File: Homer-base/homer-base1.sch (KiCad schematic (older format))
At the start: 13 parts, among them J1 J1 LEFT, J2 J2 DOWN, J3 J3 RIGHT

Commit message: Add level converter and other fix
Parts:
- removed P?: CONN_6, symbol CONN_6
- added P?: CONN_5, symbol CONN_5
- added U?: DCDC, symbol DCDC
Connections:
- net labels added: +3.6V
- wire segments 62 -> 81
- no-connect marks 0 -> 1
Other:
- moved on the sheet: C?, J?, JP?, U?

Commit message: New power supply subsystem
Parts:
- removed P?: CONN_5, symbol CONN_5
- added JP?: JUMPER, symbol JUMPER
- added P?: CONN_4, symbol CONN_4
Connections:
- net labels added: 3,3V
- net labels removed: +3,3V
- no-connect marks 1 -> 0
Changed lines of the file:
@@
 LIBS:valves
 LIBS:MyKicadLib
+LIBS:molex
 LIBS:homer-base1-cache
 EELAYER 27 0
@@
 Sheet 1 1
 Title ""
-Date "1 jan 2016"
+Date "12 feb 2017"
 Rev ""
 Comp ""
@@
 Connection ~ 6950 1450
 Wire Wire Line
-	3750 700  6650 700
-Wire Wire Line
 	6650 700  6650 950
 Wire Wire Line
@@
 Wire Wire Line
 	5200 5550 6600 5550
-Wire Wire Line
-	6300 5550 6300 5250
 Wire Wire Line
 	4900 2250 4650 2250
@@
 $EndComp
 $Comp
-L +3,3V #PWR?
-U 1 1 55470334
-P 6300 5250
-F 0 "#PWR?" H 6300 5210 30  0001 C CNN
-F 1 "+3,3V" H 6300 5360 30  0000 C CNN
-F 2 "" H 6300 5250 60  0001 C CNN
-F 3 "" H 6300 5250 60  0001 C CNN
-	1    6300 5250
-	1    0    0    -1
-$EndComp
-$Comp
 L GND #PWR?
 U 1 1 554702F9
@@
 $EndComp
 Wire Wire Line
-	1200 1100 1200 2950
+	1200 700  1200 2950
 $Comp
 L +3.3V #PWR?
@@
 $EndComp
 Wire Wire Line
-	1500 650  1500 3750
-Wire Wire Line
-	1500 700  1050 700
-Connection ~ 1500 700
+	1500 650  1500 3000
 Entry Wire Line
 	1500 3750 1600 3850
-Connection ~ 6300 5550
 Entry Wire Line
 	5100 5450 5200 5550
@@
 	3750 700  3750 2250
 Wire Wire Line
-	2450 2250 1500 2250
-Connection ~ 1500 2250
-Wire Wire Line
 	3450 2350 3750 2350
 Wire Wire Line
@@
 Wire Wire Line
 	3750 2750 1200 2750
-Connection ~ 1200 2750
 Wire Wire Line
 	2450 2350 2300 2350
@@
 	2300 2350 2300 2750
 Connection ~ 2300 2750
-$Comp
-L CONN_5 P?
-U 1 1 56866CB4
-P 650 900
-F 0 "P?" V 600 900 50  0000 C CNN
-F 1 "CONN_5" V 700 900 50  0000 C CNN
-F 2 "" H 650 900 60  0000 C CNN
-F 3 "" H 650 900 60  0000 C CNN
-	1    650  900
-	-1   0    0    -1
-$EndComp
-NoConn ~ 1050 1000
-Wire Wire Line
-	1200 1100 1050 1100
 $Comp
 L +3.6V #PWR?
@@
 $EndComp
 Wire Wire Line
-	1050 800  3750 800
-Connection ~ 3750 800
-Wire Wire Line
-	1650 800  1650 650
-Connection ~ 1650 800
+	1650 650  1650 1000
 $Comp
 L +3.6V #PWR?
@@
 	1    0    0    -1
 $EndComp
-Wire Wire Line
-	1050 900  1800 900
-Wire Wire Line
-	1800 900  1800 650
 Entry Wire Line
 	8300 1900 8400 2000
@@
 Wire Wire Line
 	10100 3000 10100 2950
+$Comp
+L JUMPER JP?
+U 1 1 58A04E2A
+P 1500 3300
+F 0 "JP?" H 1500 3450 60  0000 C CNN
+F 1 "JUMPER" H 1500 3220 40  0000 C CNN
+F 2 "" H 1500 3300 60  0001 C CNN
+F 3 "" H 1500 3300 60  0001 C CNN
+	1    1500 3300
+	0    1    1    0
+$EndComp
+Wire Wire Line
+	1500 3750 1500 3600
+Text Label 6350 5550 0    60   ~ 0
+3,3V
+Wire Wire Line
+	2450 2250 1500 2250
+Connection ~ 1500 2250
+$Comp
+L CONN_4 P?
+U 1 1 58A0935B
+P 650 850
+F 0 "P?" V 600 850 50  0000 C CNN
+F 1 "CONN_4" V 700 850 50  0000 C CNN
+F 2 "" H 650 850 60  0000 C CNN
+F 3 "" H 650 850 60  0000 C CNN
+	1    650  850
+	-1   0    0    -1
+$EndComp
+Connection ~ 3750 700
+Wire Wire Line
+	1800 650  1800 900
+Wire Wire Line
+	1650 700  6650 700
+Connection ~ 1200 2750
+Wire Wire Line
+	1200 700  1000 700
+Wire Wire Line
+	1650 1000 1000 1000
+Connection ~ 1650 700
+Wire Wire Line
+	1800 900  1000 900
+Wire Wire Line
+	1000 800  1500 800
+Connection ~ 1500 800
 $EndSCHEMATC

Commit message: Add current sensor, RTC battery, Power protection
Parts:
- added BT?: BATTERY, ~, symbol BATTERY
- added P?: BASE POWER, symbol CONN_8X2
- P?: value CONN_8X2 -> FRONT PANEL
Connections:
- net GND: now also BT?.2 (-)
- net PA30 TWD0: now also P?.2
- net PA31 TWCK0: now also P?.1
- net VBAT: now reaches J3.2 (P2)
- net VBAT: now also BT?.1 (+)
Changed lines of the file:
@@
 Sheet 1 1
 Title ""
-Date "12 feb 2017"
+Date "18 apr 2017"
 Rev ""
 Comp ""
@@
 	6900 2250 6500 2250
 Wire Wire Line
-	6950 1450 6950 1600
+	6950 850  6950 1600
 Connection ~ 6950 1450
 Wire Wire Line
@@
 	10800 3850 750  3850
 Wire Bus Line
-	10800 1850 10800 3850
+	10800 1850 10800 7000
 Wire Bus Line
 	8100 3950 8100 7000
@@
 	2400 5300 3000 5300
 Wire Bus Line
-	8300 1800 8300 3750
+	8300 700  8300 3750
 Entry Wire Line
 	3000 5400 3100 5500
@@
 P 9500 2350
 F 0 "P?" H 9500 2800 60  0000 C CNN
-F 1 "CONN_8X2" V 9500 2350 50  0000 C CNN
+F 1 "FRONT PANEL" V 9500 2350 50  0000 C CNN
 F 2 "" H 9500 2350 60  0001 C CNN
 F 3 "" H 9500 2350 60  0001 C CNN
@@
 	1000 800  1500 800
 Connection ~ 1500 800
+$Comp
+L CONN_8X2 P?
+U 1 1 58D59E38
+P 9550 5550
+F 0 "P?" H 9550 6000 60  0000 C CNN
+F 1 "BASE POWER" V 9550 5550 50  0000 C CNN
+F 2 "" H 9550 5550 60  0000 C CNN
+F 3 "" H 9550 5550 60  0000 C CNN
+	1    9550 5550
+	1    0    0    -1
+$EndComp
+Entry Wire Line
+	10700 5200 10800 5300
+Wire Wire Line
+	10700 5200 9950 5200
+Text Label 9950 5200 0    60   ~ 0
+PA30 TWD0
+Text Label 8650 5200 0    60   ~ 0
+PA31 TWCK0
+Entry Wire Line
+	10700 4900 10800 5000
+Wire Wire Line
+	8650 4900 10700 4900
+Wire Wire Line
+	8650 5200 9150 5200
+Wire Wire Line
+	8650 4900 8650 5200
+$Comp
+L BATTERY BT?
+U 1 1 58F66281
+P 7550 850
+F 0 "BT?" H 7550 1050 50  0000 C CNN
+F 1 "BATTERY" H 7550 660 50  0000 C CNN
+F 2 "~" H 7550 850 60  0000 C CNN
+F 3 "~" H 7550 850 60  0000 C CNN
+	1    7550 850
+	-1   0    0    1
+$EndComp
+Wire Wire Line
+	6950 850  7250 850
+Entry Wire Line
+	8200 850  8300 950
+Wire Wire Line
+	7850 850  8200 850
+Entry Wire Line
+	8000 4550 8100 4650
+Wire Wire Line
+	8000 4550 7400 4550
+Text Label 7450 4550 0    60   ~ 0
+VBAT
+Text Label 7950 850  0    60   ~ 0
+VBAT
 $EndSCHEMATC

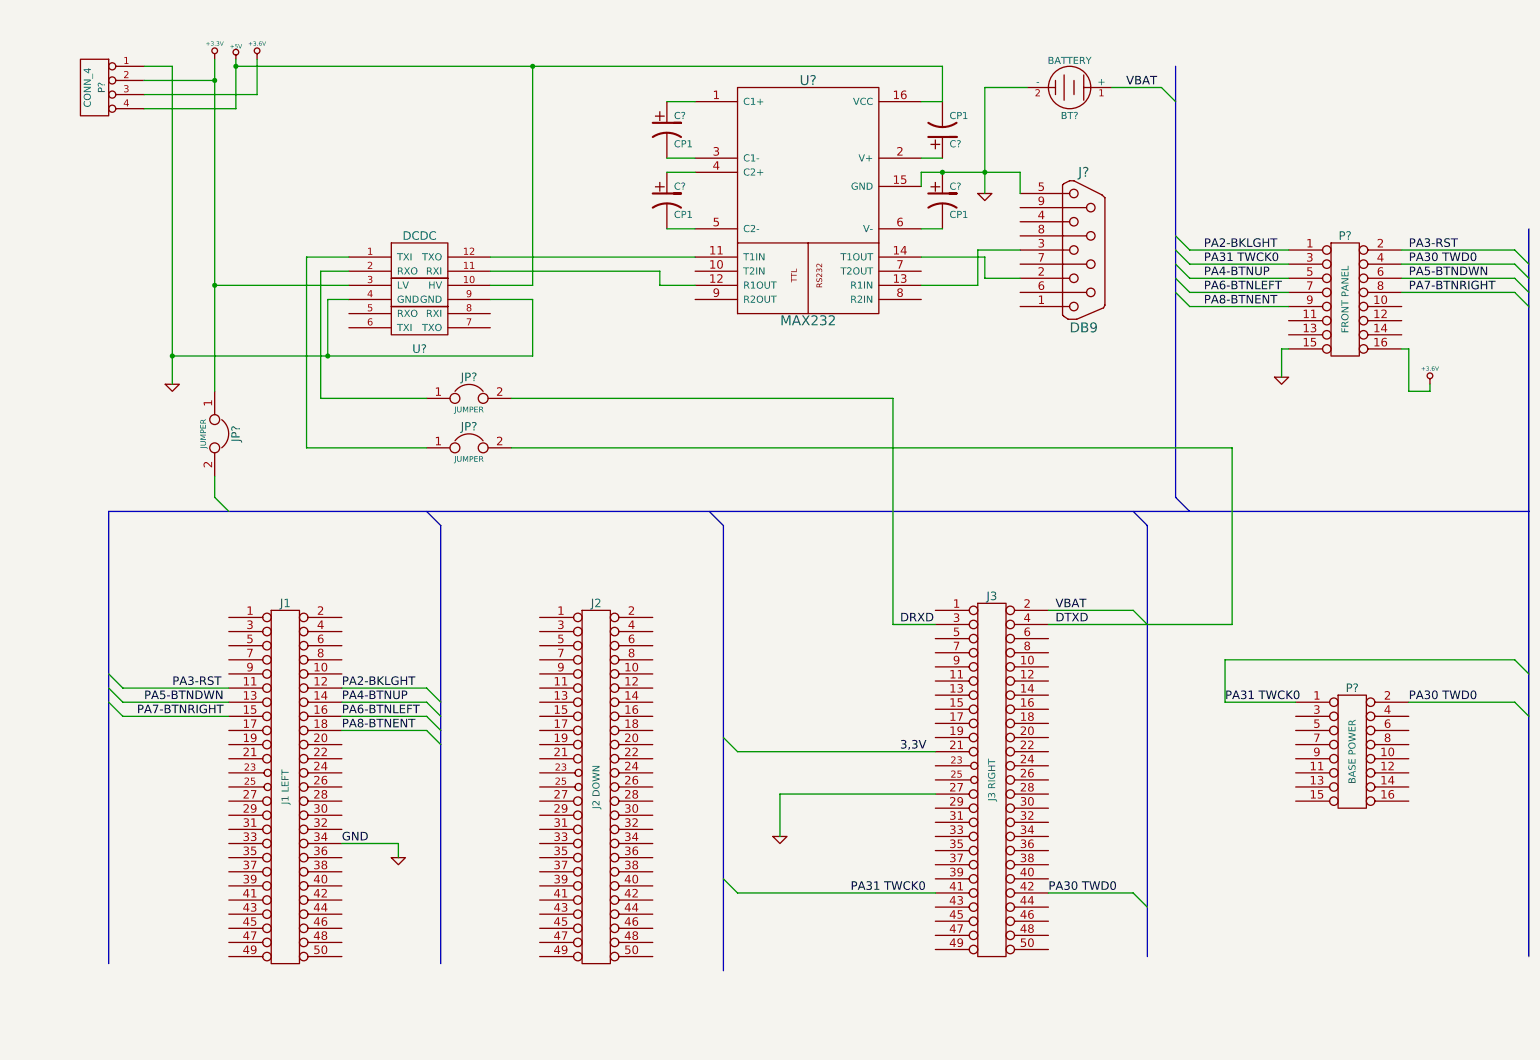
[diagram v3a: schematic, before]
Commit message: Power revision and add ina219 sensor
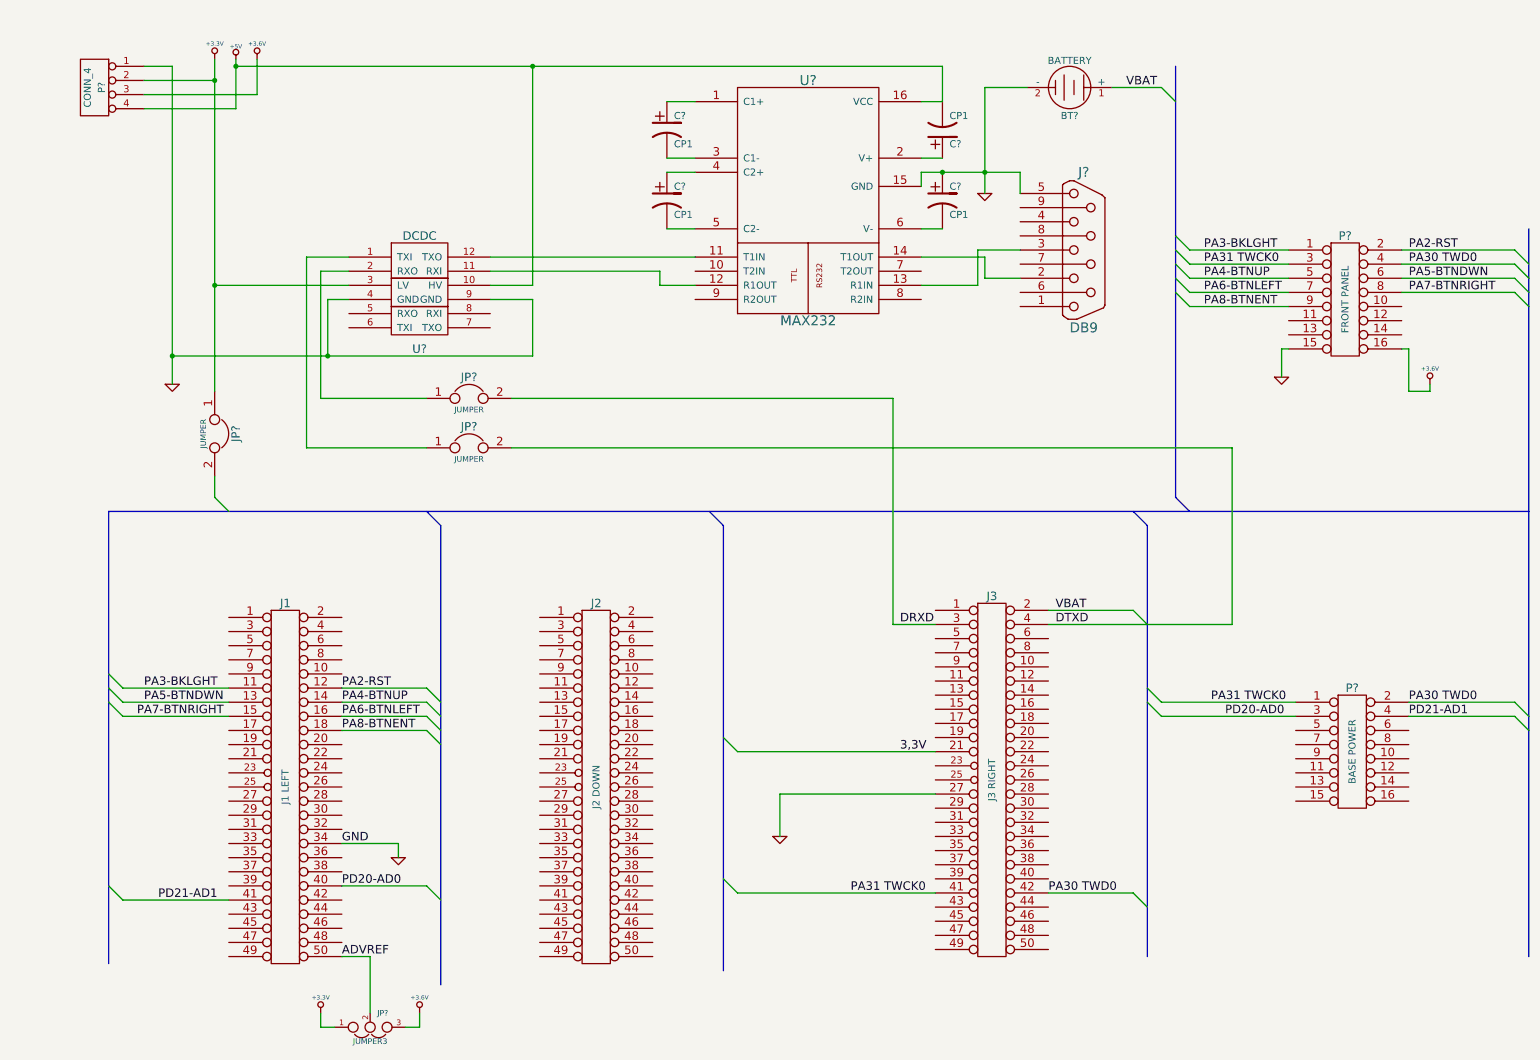
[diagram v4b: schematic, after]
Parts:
- added JP?: JUMPER3, ~, symbol JUMPER3
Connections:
- net +3.3V: now also JP?.1
- net +3.6V: now also JP?.3
- net PD20-AD0: now reaches J1.40 (P40)
- net PD20-AD0: now also P?.3
- net PD21-AD1: now reaches J1.41 (P41)
- net PD21-AD1: now also P?.4
- net ADVREF: now reaches J1.50 (P50)
- net ADVREF: now also JP?.2
- net PA2-BKLGHT renamed PA2-RST
- net PA2-RST: now also P?.2; no longer P?.1
- net PA3-RST renamed PA3-BKLGHT
- net PA3-BKLGHT: now also P?.1; no longer P?.2
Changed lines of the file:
@@
 Sheet 1 1
 Title ""
-Date "18 apr 2017"
+Date "21 apr 2017"
 Rev ""
 Comp ""
@@
 	1600 5100 850  5100
 Wire Wire Line
-	8700 3400 8700 4650
-Wire Wire Line
-	8700 4650 7400 4650
+	8700 4650 8700 3400
+Wire Wire Line
+	7400 4650 8700 4650
 Wire Wire Line
 	5500 6150 5500 5850
@@
 	1600 5200 850  5200
 Wire Bus Line
-	10800 3850 750  3850
+	750  3850 10800 3850
 Wire Bus Line
 	10800 1850 10800 7000
@@
 	6600 6550 5200 6550
 Wire Bus Line
-	3100 3950 3100 7050
+	3100 3950 3100 7200
 Wire Wire Line
 	3000 5200 2400 5200
@@
 Entry Bus Bus
 	5000 3850 5100 3950
+Text Label 1000 5100 0    60   ~ 0
+PA3-BKLGHT
 Text Label 2400 5100 0    60   ~ 0
-PA2-BKLGHT
-Text Label 1200 5100 0    60   ~ 0
-PA3-RST
+PA2-RST
 Entry Wire Line
 	750  5000 850  5100
@@
 	2150 2050 2450 2050
 Wire Wire Line
-	3600 3400 8700 3400
+	8700 3400 3600 3400
 Wire Wire Line
 	4900 2050 3450 2050
@@
 	8400 2300 9100 2300
 Text Label 8500 2000 0    60   ~ 0
-PA2-BKLGHT
+PA3-BKLGHT
 Entry Wire Line
 	10700 2000 10800 2100
@@
 	9900 2000 10700 2000
 Text Label 9950 2000 0    60   ~ 0
-PA3-RST
+PA2-RST
 Text Label 8500 2100 0    60   ~ 0
 PA31 TWCK0
@@
 Text Label 9950 5200 0    60   ~ 0
 PA30 TWD0
-Text Label 8650 5200 0    60   ~ 0
+Text Label 8550 5200 0    60   ~ 0
 PA31 TWCK0
 Entry Wire Line
-	10700 4900 10800 5000
-Wire Wire Line
-	8650 4900 10700 4900
-Wire Wire Line
-	8650 5200 9150 5200
-Wire Wire Line
-	8650 4900 8650 5200
+	8100 5100 8200 5200
+Wire Wire Line
+	8200 5200 9150 5200
 $Comp
 L BATTERY BT?
@@
 Text Label 7950 850  0    60   ~ 0
 VBAT
+Entry Wire Line
+	3000 6500 3100 6600
+Wire Wire Line
+	2400 6500 3000 6500
+Entry Wire Line
+	750  6500 850  6600
+Wire Wire Line
+	1600 6600 850  6600
+Text Label 2400 6500 0    60   ~ 0
+PD20-AD0
+Text Label 1100 6600 0    60   ~ 0
+PD21-AD1
+Text Label 2400 7000 0    60   ~ 0
+ADVREF
+Wire Wire Line
+	9150 5300 8200 5300
+Wire Wire Line
+	9950 5300 10700 5300
+Entry Wire Line
+	10700 5300 10800 5400
+Entry Wire Line
+	8100 5200 8200 5300
+Text Label 8650 5300 0    60   ~ 0
+PD20-AD0
+Text Label 9950 5300 0    60   ~ 0
+PD21-AD1
+$Comp
+L +3.3V #PWR?
+U 1 1 58F9A753
+P 2250 7400
+F 0 "#PWR?" H 2250 7360 30  0001 C CNN
+F 1 "+3.3V" H 2250 7510 30  0000 C CNN
+F 2 "" H 2250 7400 60  0000 C CNN
+F 3 "" H 2250 7400 60  0000 C CNN
+	1    2250 7400
+	1    0    0    -1
+$EndComp
+$Comp
+L +3.6V #PWR?
+U 1 1 58F9A75B
+P 2950 7400
+F 0 "#PWR?" H 2950 7360 30  0001 C CNN
+F 1 "+3.6V" H 2950 7510 30  0000 C CNN
+F 2 "" H 2950 7400 60  0000 C CNN
+F 3 "" H 2950 7400 60  0000 C CNN
+	1    2950 7400
+	1    0    0    -1
+$EndComp
+$Comp
+L JUMPER3 JP?
+U 1 1 58F9A76A
+P 2600 7500
+F 0 "JP?" H 2650 7400 40  0000 L CNN
+F 1 "JUMPER3" H 2600 7600 40  0000 C CNN
+F 2 "~" H 2600 7500 60  0000 C CNN
+F 3 "~" H 2600 7500 60  0000 C CNN
+	1    2600 7500
+	1    0    0    1
+$EndComp
+Wire Wire Line
+	2400 7000 2600 7000
+Wire Wire Line
+	2600 7000 2600 7400
+Wire Wire Line
+	2850 7500 2950 7500
+Wire Wire Line
+	2950 7500 2950 7400
+Wire Wire Line
+	2350 7500 2250 7500
+Wire Wire Line
+	2250 7500 2250 7400
 $EndSCHEMATC
